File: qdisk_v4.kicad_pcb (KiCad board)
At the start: 2 copper layers, 125.7 x 99.1 mm, 31 parts, among them J1 QL_SLOT_DIN41612_CARD, J2 Conn_02x17_Odd_Even, Q1 PN2222A, U1 7805, U3 LS03, U4 LS11, U6 LS04, U7 LS00, U8 LS240, U9 27C128, Y1 8Mhz

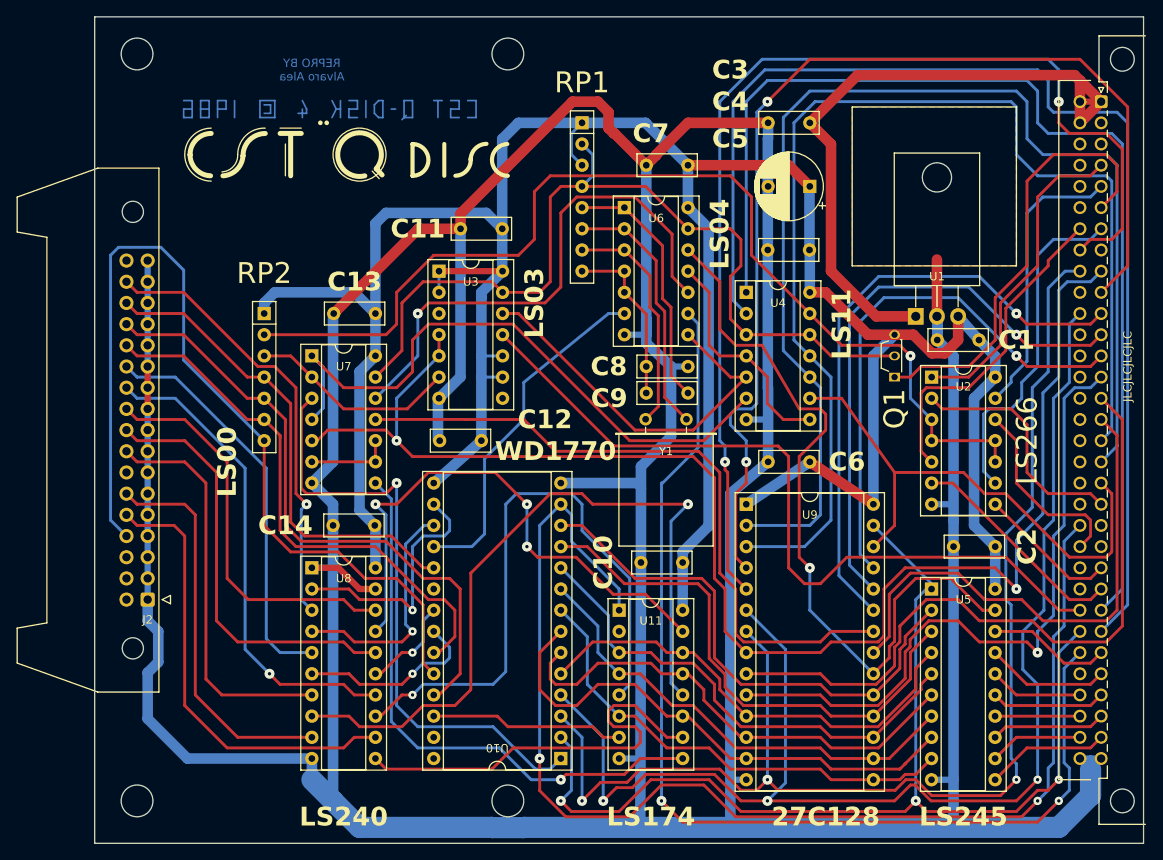
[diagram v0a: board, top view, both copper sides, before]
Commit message: Add manual, 3d case and small corrections
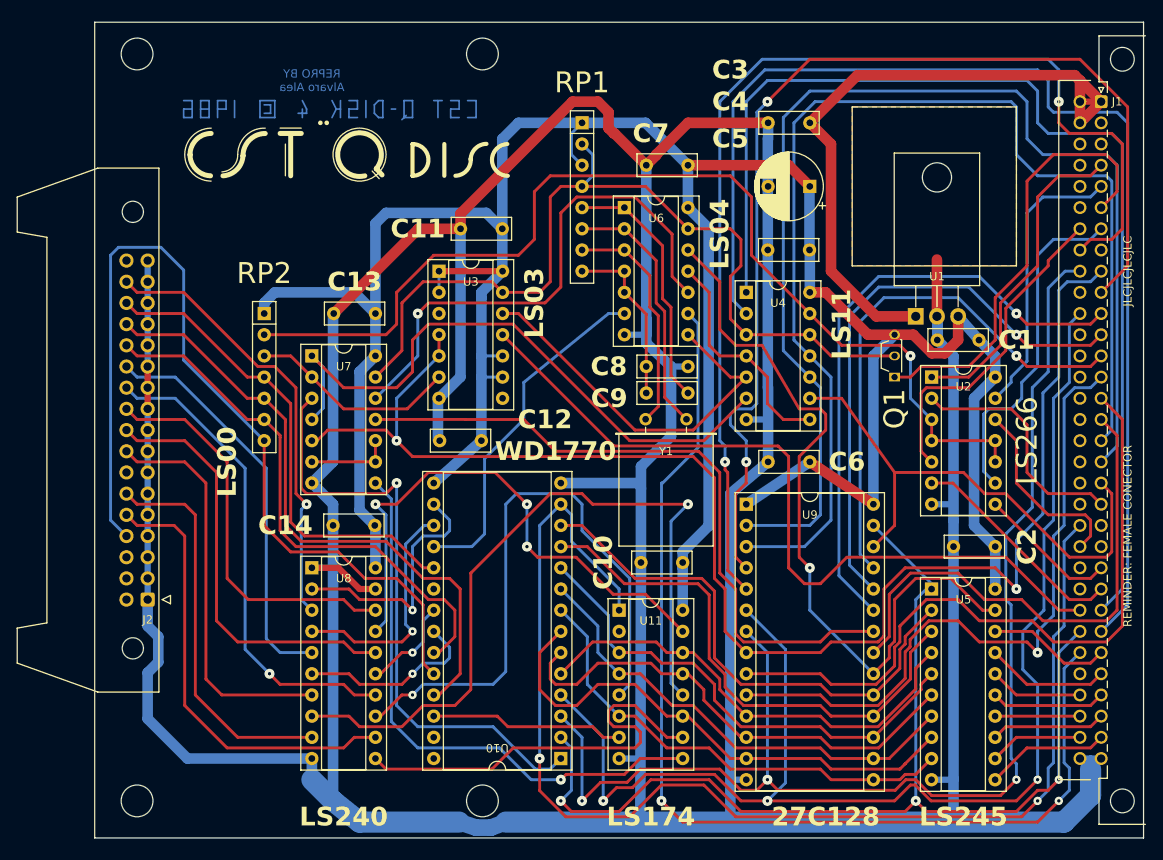
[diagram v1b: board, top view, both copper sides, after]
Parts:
- C3: value 100n -> 330nf
- C9: value 27p -> 100n
- J1: footprint Connector_DIN:DIN41612_B_2x32_Male_Horizontal_THT -> 8bits:DIN41612_B_2x32_Female_Horizontal_THT
- RP1: value R_Network08 -> 2K2 o 4K7?
- RP2: value R_Network08 -> 2K2
- moved J1 78.7 mm to (192.5, 133.2)
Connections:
- net /FDC_IP renamed /INDEX
- net /FDC_T0 renamed /TRACK_0
- net /FDC_WRP renamed /WRITE_PROT
- net /NOSE_7 renamed /A3N_PULLUP
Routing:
- net GND: track 621.9 -> 619.5 mm
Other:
- board size 125.7 x 99.1 mm -> 125.7 x 97.8 mm
- board text added: "REMINDER: FEMALE CONECTOR"

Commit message: Small corrections in the 3D model of the case
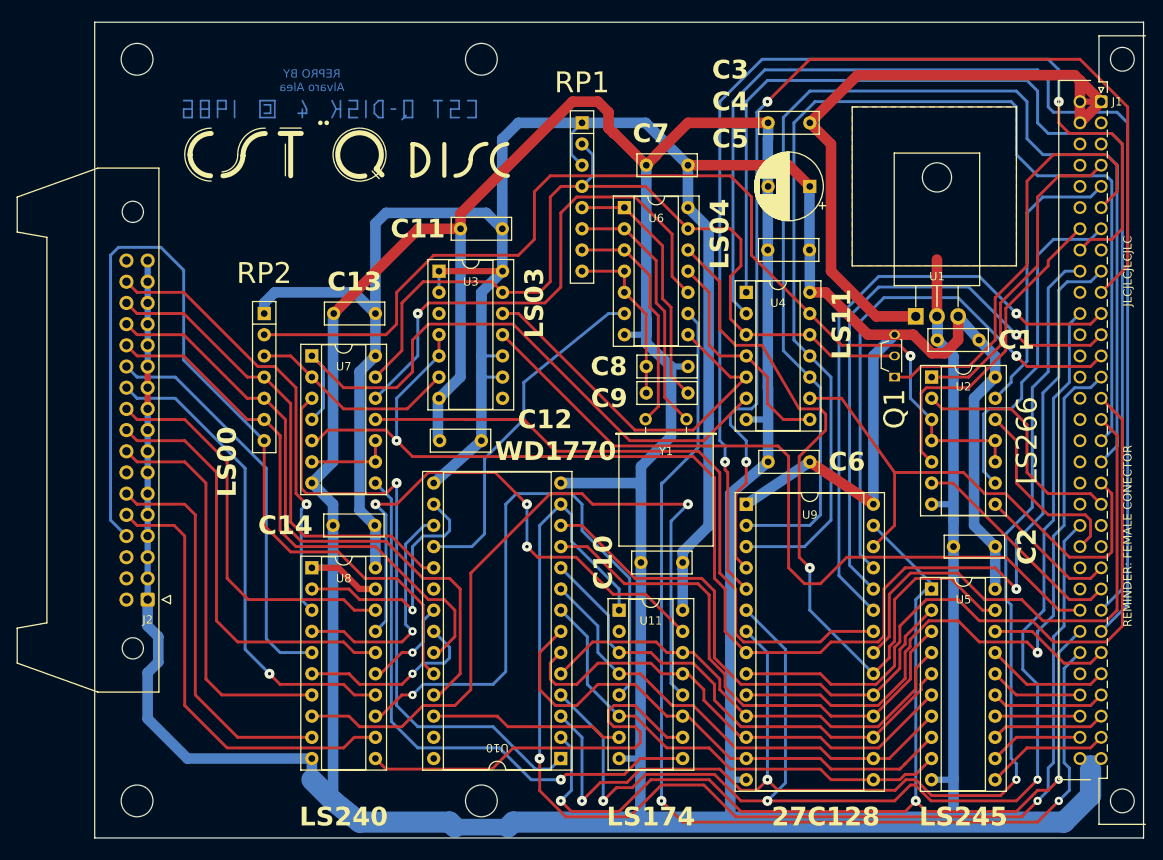
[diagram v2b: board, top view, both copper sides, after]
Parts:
- RP1: value 2K2 o 4K7? -> 4K7 (x4)
- RP2: value 2K2 -> 2K2 (x6)
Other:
- outline, holes or cut-outs redrawn
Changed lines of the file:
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@@
     (pad "" np_thru_hole circle locked (at -83.82 -2.54 270) (size 2.85 2.85) (drill 2.85) (layers "*.Cu" "*.Mask"))
     (pad "" np_thru_hole circle locked (at 5.08 -2.54 270) (size 2.85 2.85) (drill 2.85) (layers "*.Cu" "*.Mask"))
-    (pad "a1" thru_hole roundrect locked (at -78.74 0 90) (size 1.55 1.55) (drill 1) (layers "*.Cu" "*.Mask") (roundrect_rratio 0.16129)
+    (pad "a1" thru_hole roundrect locked (at -78.74 0 90) (size 1.55 1.55) (drill 1) (layers "*.Cu" "*.Mask") (roundrect_rratio 0.1612896774)
       (net 2 "+9V") (pinfunction "Vin") (pintype "passive"))
     (pad "a2" thru_hole circle locked (at -76.2 0 90) (size 1.55 1.55) (drill 1) (layers "*.Cu" "*.Mask")
@@
         (effects (font (size 2.5 2.5) (thickness 0.4)))
     )
-    (fp_text value "2K2 o 4K7?" (at 10.16 2.4 -90) (layer "F.Fab")
+    (fp_text value "4K7 (x4)" (at 10.16 2.4 -90) (layer "F.Fab")
         (effects (font (size 1 1) (thickness 0.15)))
     )
@@
         (effects (font (size 2.5 2.5) (thickness 0.4)))
     )
-    (fp_text value "2K2" (at 8.89 2.4 -90) (layer "F.Fab")
+    (fp_text value "2K2 (x6)" (at 8.89 2.4 -90) (layer "F.Fab")
         (effects (font (size 1 1) (thickness 0.15)))
     )
@@
   (gr_circle (center 76.454 120.015) (end 77.724 120.015)
     (stroke (width 0.05) (type solid)) (fill none) (layer "Edge.Cuts"))
-  (gr_circle (center 76.962 48.768) (end 78.867 48.768)
+  (gr_circle (center 76.962 49.403) (end 78.867 49.403)
     (stroke (width 0.05) (type solid)) (fill none) (layer "Edge.Cuts"))
-  (gr_circle (center 118.364 138.303) (end 120.269 138.303)
+  (gr_circle (center 118.237 138.303) (end 120.142 138.303)
     (stroke (width 0.05) (type solid)) (fill none) (layer "Edge.Cuts"))
   (gr_line (start 197.612 142.748) (end 197.612 44.958)
@@
   (gr_line (start 71.882 44.958) (end 71.882 142.748)
     (stroke (width 0.05) (type solid)) (layer "Edge.Cuts"))
-  (gr_circle (center 118.364 48.768) (end 120.269 48.768)
+  (gr_circle (center 118.237 49.403) (end 120.142 49.403)
     (stroke (width 0.05) (type solid)) (fill none) (layer "Edge.Cuts"))
   (gr_line (start 71.882 142.748) (end 197.612 142.748)
@@
   (segment (start 134.192 58.293) (end 138.002 62.103) (width 1.27) (layer "F.Cu") (net 1))
   (segment (start 134.747 133.223) (end 137.367 133.223) (width 0.75) (layer "B.Cu") (net 1))
-  (segment (start 117.602 141.507558) (end 119.38 141.507558) (width 2) (layer "B.Cu") (net 1))
   (segment (start 174.832 85.003) (end 172.887 83.058) (width 1.27) (layer "B.Cu") (net 1))
   (segment (start 138.002 80.518) (end 138.002 82.503) (width 1.27) (layer "B.Cu") (net 1))
@@
   (segment (start 78.232 128.4605) (end 82.9945 133.223) (width 1.27) (layer "B.Cu") (net 1))
   (segment (start 152.567 58.968) (end 152.567 72.263) (width 1.27) (layer "B.Cu") (net 1))
-  (segment (start 188.087 140.843) (end 191.262 137.668) (width 2.54) (layer "B.Cu") (net 1))
   (segment (start 191.262 133.223) (end 192.532 133.223) (width 0.75) (layer "B.Cu") (net 1))
   (segment (start 174.832 102.823) (end 174.832 104.728) (width 0.75) (layer "B.Cu") (net 1))
   (segment (start 79.502 121.666) (end 78.232 122.936) (width 1.27) (layer "B.Cu") (net 1))
   (segment (start 174.752 102.743) (end 174.832 102.823) (width 0.75) (layer "B.Cu") (net 1))
-  (segment (start 115.57 140.843) (end 103.632 140.843) (width 2.54) (layer "B.Cu") (net 1))
   (segment (start 115.697 87.503) (end 115.737 87.503) (width 0.75) (layer "B.Cu") (net 1))
   (segment (start 100.457 97.658) (end 97.917 100.198) (width 1.27) (layer "B.Cu") (net 1))
@@
   (segment (start 78.232 114.173) (end 78.232 91.313) (width 0.75) (layer "B.Cu") (net 1))
   (segment (start 152.607 97.663) (end 152.607 88.773) (width 1.27) (layer "B.Cu") (net 1))
-  (segment (start 103.632 140.843) (end 100.457 138.303) (width 2.54) (layer "B.Cu") (net 1))
   (segment (start 172.197 135.768) (end 174.747 135.768) (width 0.75) (layer "B.Cu") (net 1))
   (segment (start 97.917 133.223) (end 97.917 135.763) (width 1.27) (layer "B.Cu") (net 1))
@@
   (segment (start 138.002 62.103) (end 138.002 80.518) (width 1.27) (layer "B.Cu") (net 1))
   (segment (start 143.002 86.233) (end 140.97 86.233) (width 0.75) (layer "B.Cu") (net 1))
-  (segment (start 121.158 140.843) (end 188.087 140.843) (width 2.54) (layer "B.Cu") (net 1))
+  (segment (start 122.047 140.843) (end 188.087 140.843) (width 2.54) (layer "B.Cu") (net 1))
   (segment (start 137.367 109.728) (end 137.287 140.843) (width 1.27) (layer "B.Cu") (net 1))
   (segment (start 113.157 90.043) (end 115.697 87.503) (width 1.27) (layer "B.Cu") (net 1))
@@
   (segment (start 152.567 72.263) (end 152.567 88.733) (width 1.27) (layer "B.Cu") (net 1))
   (segment (start 149.987 92.583) (end 152.607 92.583) (width 0.75) (layer "B.Cu") (net 1))
-  (segment (start 191.262 137.668) (end 191.262 134.493) (width 2.54) (layer "B.Cu") (net 1))
   (segment (start 137.367 100.838) (end 137.367 98.218) (width 1.27) (layer "B.Cu") (net 1))
   (segment (start 148.082 135.763) (end 149.987 135.763) (width 0.75) (layer "B.Cu") (net 1))
-  (segment (start 119.38 141.507558) (end 121.158 140.843) (width 2) (layer "B.Cu") (net 1))
   (segment (start 174.832 107.823) (end 174.832 135.683) (width 1.27) (layer "B.Cu") (net 1))
   (segment (start 152.607 58.928) (end 152.607 57.023) (width 1.27) (layer "B.Cu") (net 1))
@@
   (segment (start 78.232 117.348) (end 79.502 118.618) (width 1.27) (layer "B.Cu") (net 1))
   (segment (start 174.832 104.728) (end 174.832 107.823) (width 1.27) (layer "B.Cu") (net 1))
+  (segment (start 122.047 140.843) (end 121.437 141.453) (width 2.54) (layer "B.Cu") (net 1))
   (segment (start 172.887 82.423) (end 172.887 80.263) (width 1.27) (layer "B.Cu") (net 1))
   (segment (start 127.762 100.203) (end 137.287 100.203) (width 1.27) (layer "B.Cu") (net 1))
@@
   (segment (start 135.382 82.423) (end 137.922 82.423) (width 0.75) (layer "B.Cu") (net 1))
   (segment (start 174.832 104.728) (end 174.832 85.003) (width 1.27) (layer "B.Cu") (net 1))
+  (segment (start 100.457 138.303) (end 103.632 140.843) (width 2.54) (layer "B.Cu") (net 1))
   (segment (start 174.832 135.683) (end 174.832 140.843) (width 1.27) (layer "B.Cu") (net 1))
   (segment (start 172.212 102.743) (end 174.752 102.743) (width 0.75) (layer "B.Cu") (net 1))
+  (segment (start 103.632 140.843) (end 114.427 140.843) (width 2.54) (layer "B.Cu") (net 1))
+  (segment (start 188.087 140.843) (end 191.262 137.668) (width 2.54) (layer "B.Cu") (net 1))
+  (segment (start 114.427 140.843) (end 115.062 141.453) (width 2.54) (layer "B.Cu") (net 1))
   (segment (start 137.367 98.218) (end 140.97 94.615) (width 1.27) (layer "B.Cu") (net 1))
   (segment (start 79.502 118.618) (end 79.502 121.666) (width 1.27) (layer "B.Cu") (net 1))
   (segment (start 189.992 133.223) (end 191.262 133.223) (width 0.75) (layer "B.Cu") (net 1))
+  (segment (start 191.262 137.668) (end 191.262 134.493) (width 2.54) (layer "B.Cu") (net 1))
   (segment (start 100.457 97.658) (end 100.457 79.883) (width 1.27) (layer "B.Cu") (net 1))
   (segment (start 137.287 100.203) (end 137.367 100.283) (width 0.75) (layer "B.Cu") (net 1))
@@
   (segment (start 137.922 82.423) (end 138.002 82.503) (width 0.75) (layer "B.Cu") (net 1))
   (segment (start 100.457 102.738) (end 97.917 100.198) (width 1.27) (layer "B.Cu") (net 1))
+  (segment (start 115.062 141.453) (end 121.437 141.453) (width 2) (layer "B.Cu") (net 1))
   (segment (start 82.9945 133.223) (end 97.917 133.223) (width 1.27) (layer "B.Cu") (net 1))
   (segment (start 97.917 135.763) (end 100.457 138.303) (width 2.54) (layer "B.Cu") (net 1))
-  (segment (start 115.57 140.843) (end 117.602 141.507558) (width 2) (layer "B.Cu") (net 1))
   (segment (start 189.992 57.023) (end 189.992 54.483) (width 1.27) (layer "F.Cu") (net 2))
   (segment (start 189.992 51.943) (end 189.992 54.483) (width 1.27) (layer "F.Cu") (net 2))
